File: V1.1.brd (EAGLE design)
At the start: 15 x 35 mm, 28 parts, among them U1 AP63205WU-7SOIC_05WU-7_DIO-M, U3 ATTINY828-AU32A_ATM-M

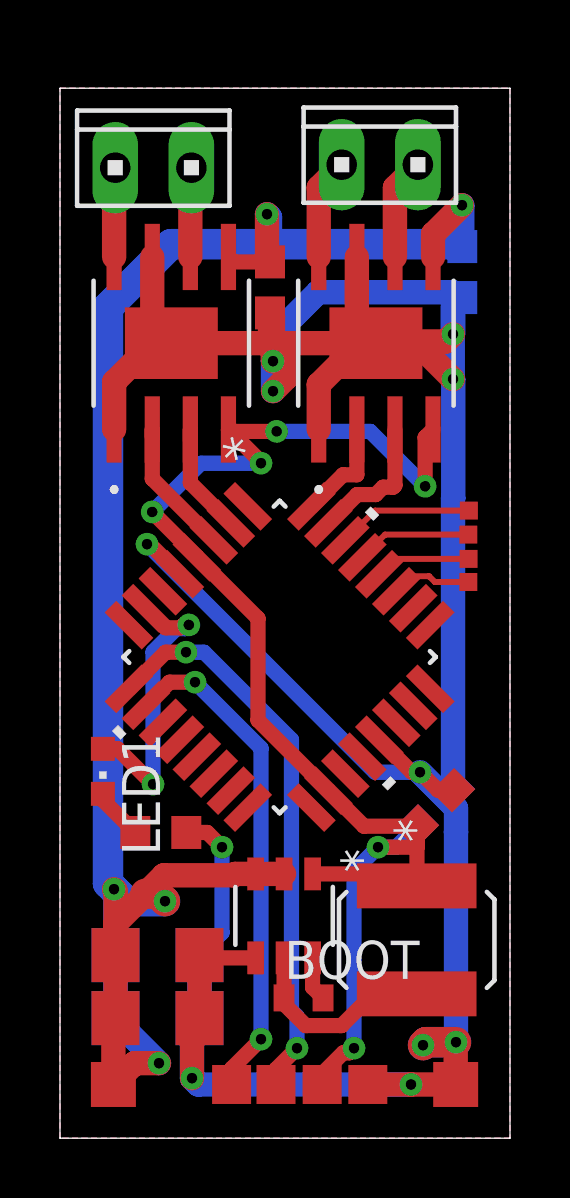
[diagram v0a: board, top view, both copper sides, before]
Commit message: V1.2
El esquemático es el mismo, la placa tiene mejores tolerancias, mejor distribución nuevos pads para señales y cumple con las especificaciones de jlcpcb
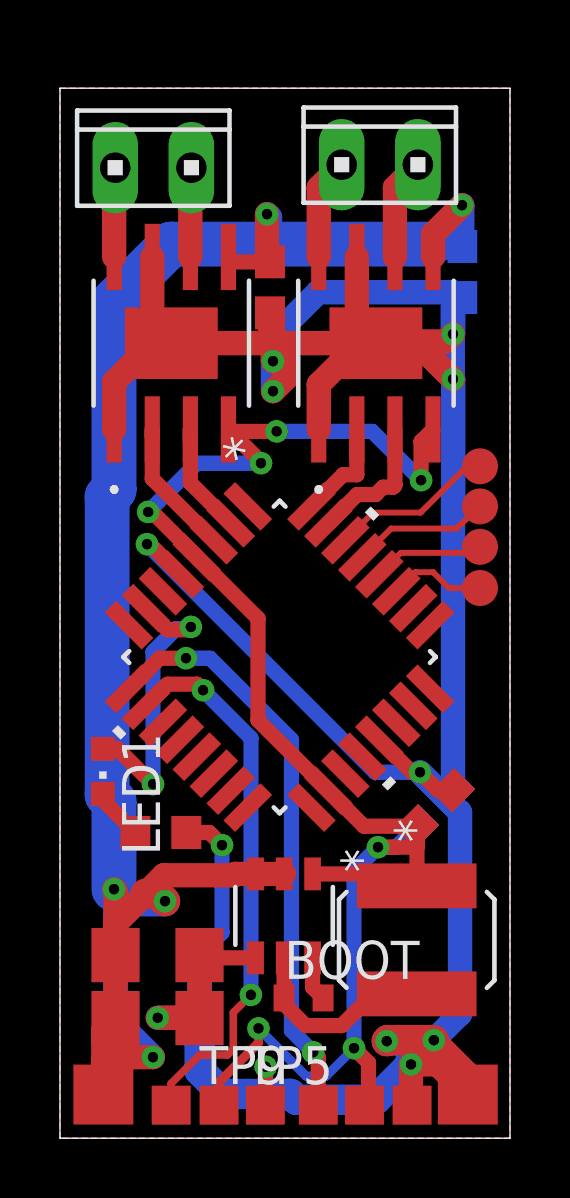
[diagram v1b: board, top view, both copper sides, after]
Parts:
- added TP5, TP9: TPTP13SQ, testpad:TP13SQ
- GND, V+: value TPTP15SQ -> TPTP20SQ; device testpad:TP15SQ -> testpad:TP20SQ
- MISO, TP6, TP7, TP8: value TPTP06SQ -> TPTP12R; device testpad:TP06SQ -> testpad:TP12R
- moved TP2 2.13 mm to (3.71, 1.10)
- moved TP4 1.63 mm to (11.7, 1.10)
- moved TP3 1.57 mm to (10.1, 1.10)
- moved TP1 1.57 mm to (8.61, 1.10)
- moved TP8 1.52 mm to (14.0, 22.4)
- moved TP7 1.02 mm to (14.0, 21.1)
- moved TP6 0.55 mm to (14.0, 19.7)
- moved GND 0.52 mm to (13.6, 1.45)
- moved V+ 0.47 mm to (1.44, 1.45)
- moved MISO 0.44 mm to (14.0, 18.3)
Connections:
- net +5V: now also TP9.TP
- net GND: now also TP5.TP
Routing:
- net +5V: track 47.5 -> 55.3 mm, vias 6 -> 7
- net GND: track 115.2 -> 122.0 mm, vias 11 -> 12
- net CANAL2: track 16.7 -> 18.4 mm
- net SCK: track 4.53 -> 5.51 mm
- net RESET: track 3.85 -> 4.61 mm
- net MOSI: track 2.69 -> 3.27 mm
- net MISO: track 3.19 -> 3.72 mm
- net CANAL1: track 19.0 -> 19.5 mm

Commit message: Add files via upload
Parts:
- removed TP2: TPTP13SQ, testpad:TP13SQ
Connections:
- removed net CANAL2: TP2.TP, U3.10
- removed net N$7: DRIVERMOTOR1.8, MOTOR1.2
- removed net N$8: DRIVERMOTOR1.6, MOTOR1.1
- net N$5: now also DRIVERMOTOR1.8, MOTOR1.2
- net N$6: now also DRIVERMOTOR1.6, MOTOR1.1
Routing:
- net CANAL2: track 18.4 -> 0.00 mm, vias 2 -> 0
- net N$6: track 3.39 -> 16.2 mm
- net N$5: track 3.39 -> 16.1 mm
- net N$8: track 2.99 -> 0.00 mm
- net N$7: track 2.99 -> 0.00 mm
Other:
- board size 15 x 35 mm -> 15 x 35.9 mm
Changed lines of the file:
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@@
 <?xml version="1.0" encoding="utf-8"?>
 <!DOCTYPE eagle SYSTEM "eagle.dtd">
-<eagle version="9.5.1">
+<eagle version="9.6.2">
 <drawing>
 <settings>
@@
 <plain>
 <wire x1="0" y1="0" x2="15" y2="0" width="0" layer="20"/>
-<wire x1="15" y1="0" x2="15" y2="35" width="0" layer="20"/>
-<wire x1="15" y1="35" x2="0" y2="35" width="0" layer="20"/>
-<wire x1="0" y1="35" x2="0" y2="0" width="0" layer="20"/>
+<wire x1="15" y1="0" x2="15" y2="35.939596875" width="0" layer="20"/>
+<wire x1="15" y1="35.939596875" x2="0" y2="35.939596875" width="0" layer="20"/>
+<wire x1="0" y1="35.939596875" x2="0" y2="0" width="0" layer="20"/>
 <rectangle x1="16.510059375" y1="18.255015625" x2="16.644259375" y2="18.322134375" layer="22" rot="R90"/>
 <rectangle x1="16.543559375" y1="18.959715625" x2="16.610759375" y2="19.026834375" layer="22" rot="R90"/>
@@
 <attribute name="VALUE" x="7.97439375" y="0.338" size="0.0254" layer="27"/>
 </element>
-<element name="TP2" library="testpad" library_urn="urn:adsk.eagle:library:385" package="TP13SQ" package3d_urn="urn:adsk.eagle:package:27974/1" value="TPTP13SQ" x="3.70658125" y="1.1" smashed="yes">
-<attribute name="POPULARITY" value="0" x="34.18658125" y="-45.89" size="1.778" layer="27" display="off"/>
-<attribute name="TP_SIGNAL_NAME" value="" x="3.70658125" y="-1.44" size="1" layer="37"/>
-<attribute name="VALUE" x="3.07158125" y="0.338" size="0.0254" layer="27"/>
-</element>
 <element name="TP3" library="testpad" library_urn="urn:adsk.eagle:library:385" package="TP13SQ" package3d_urn="urn:adsk.eagle:package:27974/1" value="TPTP13SQ" x="10.149396875" y="1.1" smashed="yes">
 <attribute name="POPULARITY" value="0" x="45.709396875" y="-45.89" size="1.778" layer="27" display="off"/>
@@
 <contactref element="DRIVERMOTOR2" pad="8"/>
 <contactref element="MOTOR2" pad="2"/>
-<wire x1="8.625" y1="29.375" x2="8.625" y2="31.685" width="0.8128" layer="1"/>
-<wire x1="8.625" y1="31.685" x2="9.39" y2="32.45" width="0.8128" layer="1"/>
+<contactref element="DRIVERMOTOR1" pad="8"/>
+<contactref element="MOTOR1" pad="2"/>
+<wire x1="2.783" y1="33.7735" x2="3.7185" y2="34.709" width="1.27" layer="1"/>
+<wire x1="3.7185" y1="34.709" x2="5.0415" y2="34.709" width="1.27" layer="1"/>
+<wire x1="2.783" y1="33.293" x2="2.783" y2="33.7735" width="1.27" layer="1"/>
+<wire x1="7.3005" y1="32.45" x2="9.39" y2="32.45" width="1.27" layer="1"/>
+<wire x1="1.84" y1="32.35" x2="2.783" y2="33.293" width="1.27" layer="1"/>
+<wire x1="5.0415" y1="34.709" x2="7.3005" y2="32.45" width="1.27" layer="1"/>
+<wire x1="9.39" y1="32.45" x2="8.625" y2="31.685" width="1.016" layer="1"/>
+<wire x1="8.625" y1="31.685" x2="8.625" y2="29.375" width="1.016" layer="1"/>
+<wire x1="1.84" y1="32.35" x2="1.805" y2="32.315" width="1.016" layer="1"/>
+<wire x1="1.805" y1="32.315" x2="1.805" y2="29.375" width="1.016" layer="1"/>
 </signal>
 <signal name="N$6">
 <contactref element="DRIVERMOTOR2" pad="6"/>
 <contactref element="MOTOR2" pad="1"/>
-<wire x1="11.165" y1="29.375" x2="11.165" y2="31.685" width="0.8128" layer="1"/>
-<wire x1="11.165" y1="31.685" x2="11.93" y2="32.45" width="0.8128" layer="1"/>
-</signal>
-<signal name="N$7">
-<contactref element="DRIVERMOTOR1" pad="8"/>
-<contactref element="MOTOR1" pad="2"/>
-<wire x1="1.84" y1="32.35" x2="1.805" y2="32.315" width="0.8128" layer="1"/>
-<wire x1="1.805" y1="32.315" x2="1.805" y2="29.375" width="0.8128" layer="1"/>
-</signal>
-<signal name="N$8">
 <contactref element="DRIVERMOTOR1" pad="6"/>
 <contactref element="MOTOR1" pad="1"/>
-<wire x1="4.38" y1="32.35" x2="4.345" y2="32.315" width="0.8128" layer="1"/>
-<wire x1="4.345" y1="32.315" x2="4.345" y2="29.375" width="0.8128" layer="1"/>
+<wire x1="10.0515" y1="34.809" x2="10.987" y2="33.8735" width="1.27" layer="16"/>
+<wire x1="10.987" y1="33.8735" x2="10.987" y2="33.393" width="1.27" layer="16"/>
+<wire x1="10.987" y1="33.393" x2="11.93" y2="32.45" width="1.27" layer="16"/>
+<wire x1="4.38" y1="32.35" x2="6.839" y2="34.809" width="1.27" layer="16"/>
+<wire x1="6.839" y1="34.809" x2="10.0515" y2="34.809" width="1.27" layer="16"/>
+<wire x1="4.38" y1="32.35" x2="4.345" y2="32.315" width="1.016" layer="1"/>
+<wire x1="4.345" y1="32.315" x2="4.345" y2="29.375" width="1.016" layer="1"/>
+<wire x1="11.93" y1="32.45" x2="11.165" y2="31.685" width="1.016" layer="1"/>
+<wire x1="11.165" y1="31.685" x2="11.165" y2="29.375" width="1.016" layer="1"/>
 </signal>
 <signal name="GND">
@@
 <polygon width="0.2" layer="16">
 <vertex x="0" y="0"/>
-<vertex x="0" y="35"/>
-<vertex x="15" y="35"/>
+<vertex x="0" y="35.939596875"/>
+<vertex x="15" y="35.939596875"/>
 <vertex x="15" y="0"/>
 </polygon>
@@
 <polygon width="0.2" layer="1">
 <vertex x="0" y="0"/>
-<vertex x="0" y="35"/>
-<vertex x="15" y="35"/>
+<vertex x="0" y="35.93959375"/>
+<vertex x="15" y="35.93959375"/>
 <vertex x="15" y="0"/>
 </polygon>
@@
 <wire x1="8.201403125" y1="2.0680625" x2="8.8680625" y2="2.0680625" width="0.3048" layer="16"/>
 <wire x1="8.8680625" y1="2.0680625" x2="9.8" y2="3" width="0.3048" layer="16"/>
-<wire x1="11.69105" y1="8.60895" x2="10.805353125" y2="8.791934375" width="0" layer="19" extent="1-1"/>
 </signal>
 <signal name="V+">
@@
 <wire x1="8.42" y1="5.024228125" x2="8.76845625" y2="4.675771875" width="0.508" layer="1"/>
 </signal>
-<signal name="CANAL2">
-<contactref element="TP2" pad="TP"/>
-<contactref element="U3" pad="10"/>
-<via x="6.36443125" y="4.776509375" extent="1-16" drill="0.35"/>
-<wire x1="6.36443125" y1="4.776509375" x2="6.36443125" y2="13.33556875" width="0.508" layer="16"/>
-<wire x1="6.36443125" y1="13.33556875" x2="4.76845625" y2="14.93154375" width="0.508" layer="16"/>
-<via x="4.76845625" y="14.93154375" extent="1-16" drill="0.35"/>
-<wire x1="4.76845625" y1="14.93154375" x2="4.567115625" y2="15.132884375" width="0.508" layer="1"/>
-<wire x1="4.567115625" y1="15.132884375" x2="3.58445625" y2="15.132884375" width="0.508" layer="1"/>
-<wire x1="3.58445625" y1="15.132884375" x2="2.865225" y2="14.413653125" width="0.508" layer="1"/>
-<wire x1="3.70658125" y1="1.1" x2="3.70658125" y2="1.8273875" width="0.254" layer="1"/>
-<wire x1="5.58545" y1="2.773" x2="5.777" y2="2.96455" width="0.254" layer="1"/>
-<wire x1="5.777" y1="2.96455" x2="5.777" y2="4.189078125" width="0.254" layer="1"/>
-<wire x1="5.777" y1="4.189078125" x2="6.36443125" y2="4.776509375" width="0.254" layer="1"/>
-<wire x1="4.65219375" y1="2.773" x2="5.58545" y2="2.773" width="0.254" layer="1"/>
-<wire x1="3.70658125" y1="1.8273875" x2="4.65219375" y2="2.773" width="0.254" layer="1"/>
-</signal>
 </signals>
